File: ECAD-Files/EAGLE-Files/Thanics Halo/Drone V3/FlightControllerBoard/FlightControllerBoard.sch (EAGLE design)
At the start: 112 parts, among them J12 UE27AE54100, J4 UE27AE54100, J5 U.FL, J7 62674-301121ALF, J8 MICROSD, T1 ALT4532M, T2 ALT4532M, U3 MPL115A2, U4 NEO-M8, U5 AZ1117EH-1.8, U7 PDDL2450, U8 74HC4053

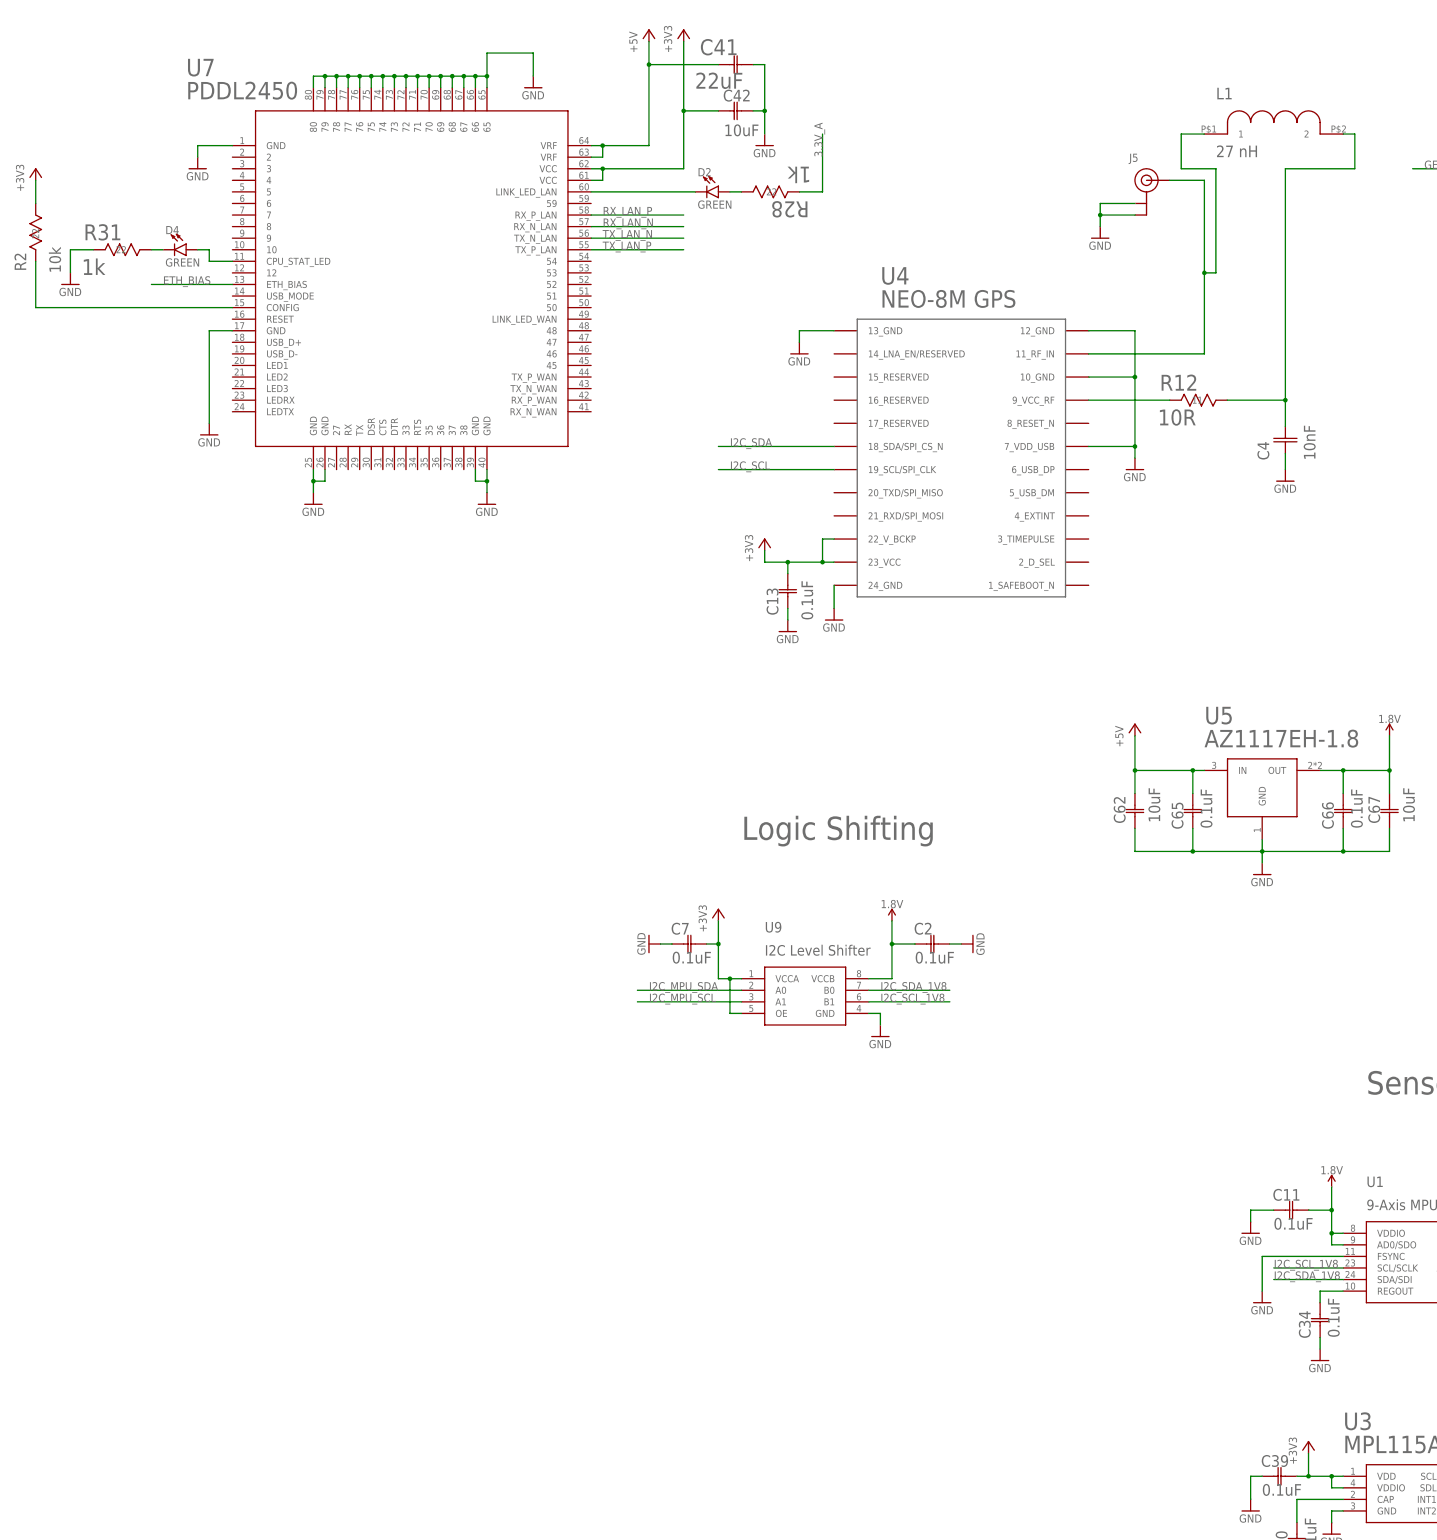
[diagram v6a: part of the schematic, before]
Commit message: About to remove touchscreen from controller board
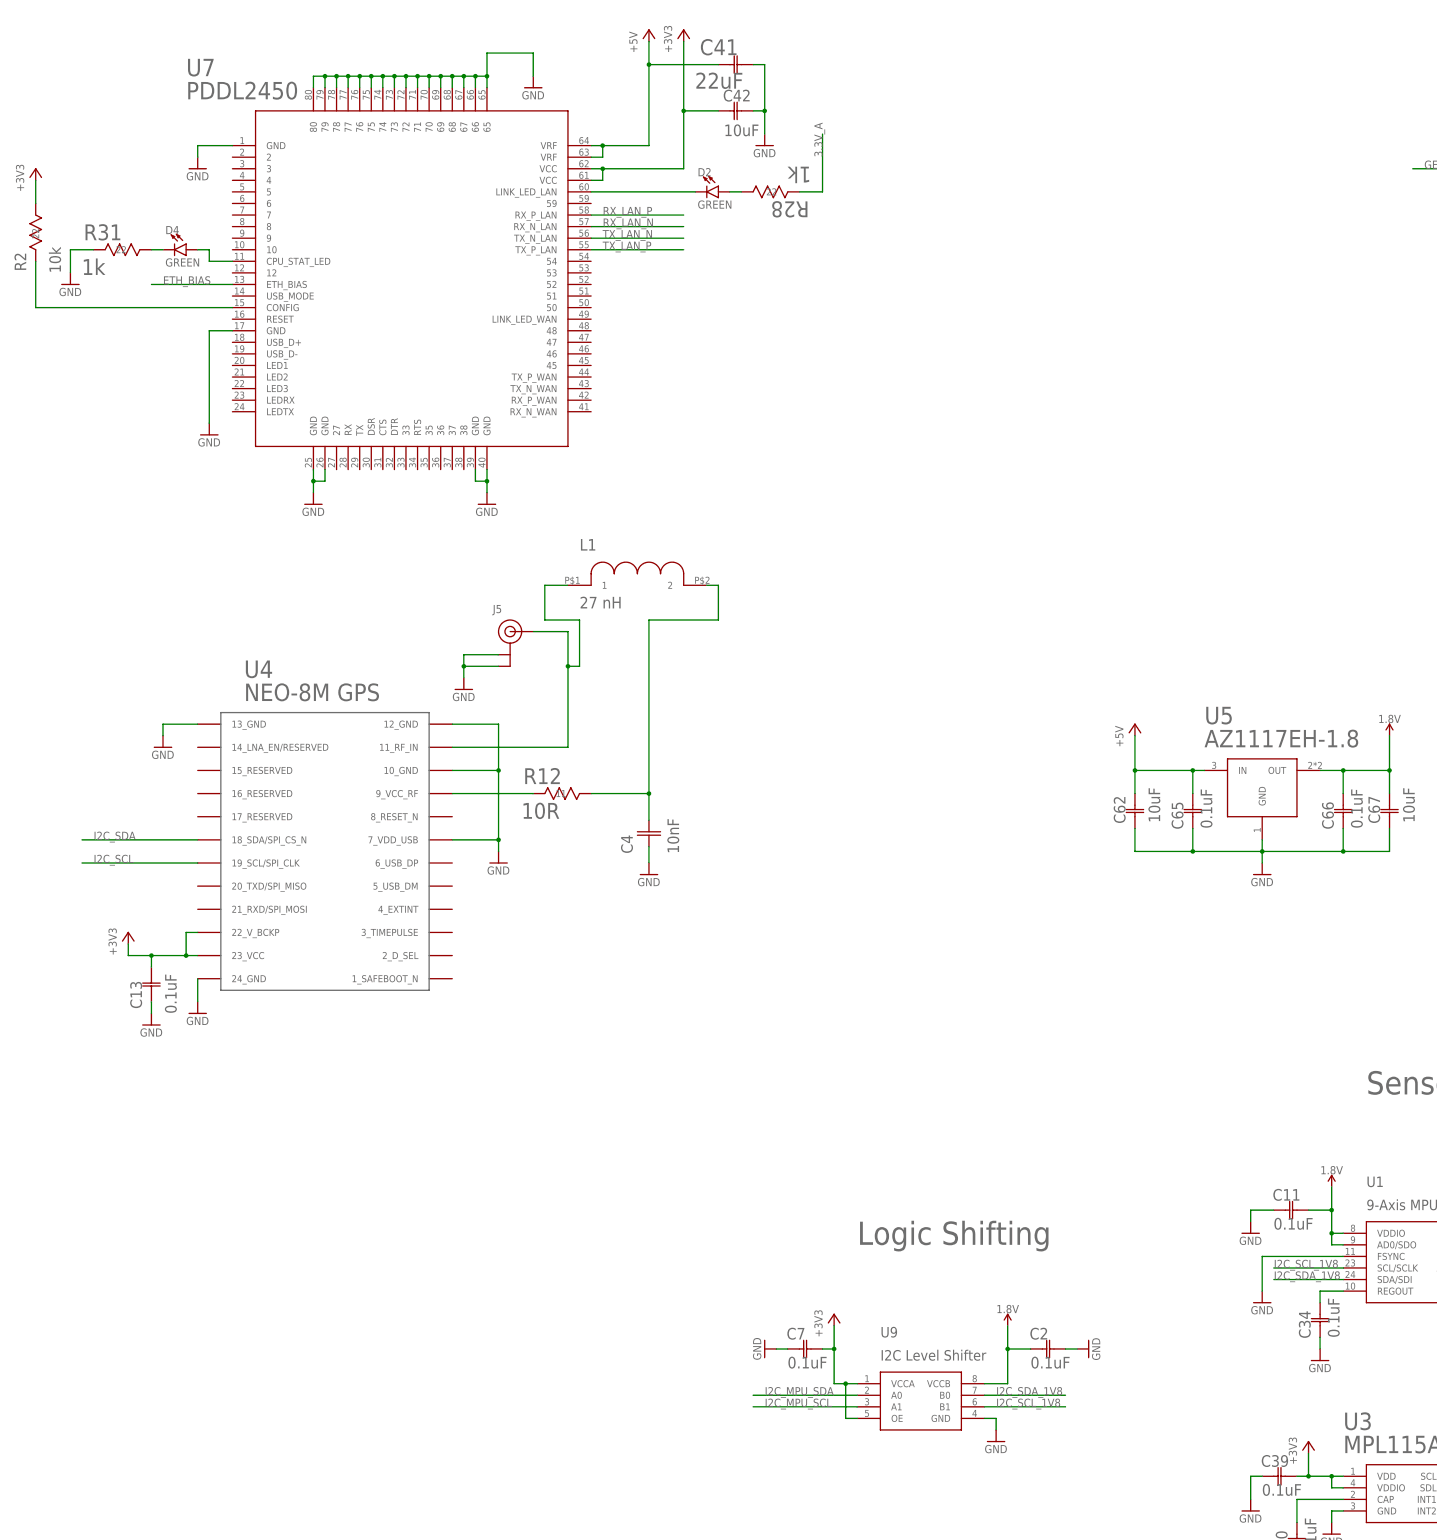
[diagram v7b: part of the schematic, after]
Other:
- moved on the sheet: C13, C2, C4, C7, J5, L1, R12, U4, U9
